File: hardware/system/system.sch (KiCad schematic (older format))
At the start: 20 parts, among them J1 CART_SOCKET_28P, J2 EXT_PINS, SW1 POWER, SW2 RESET, SW3 A, SW4 B, SW5 UP, SW6 DN, SW7 LF, SW8 RT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

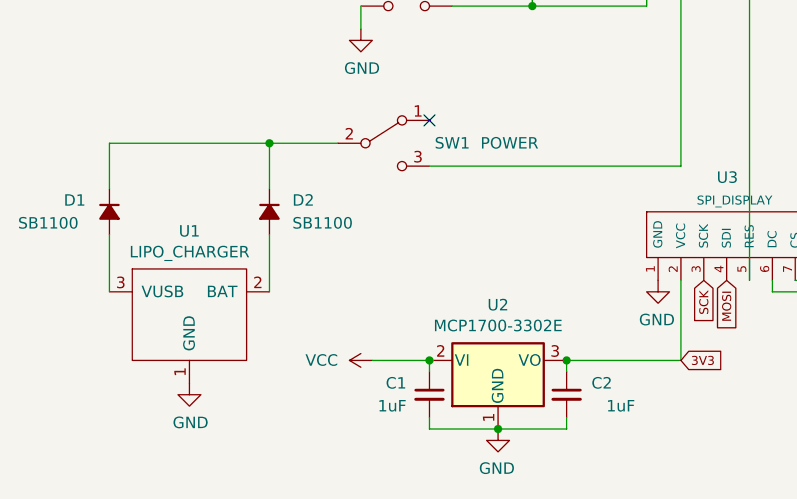
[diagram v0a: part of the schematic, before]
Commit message: Rewire screen regulator Vin to RAW
- Also add schematic PDFs
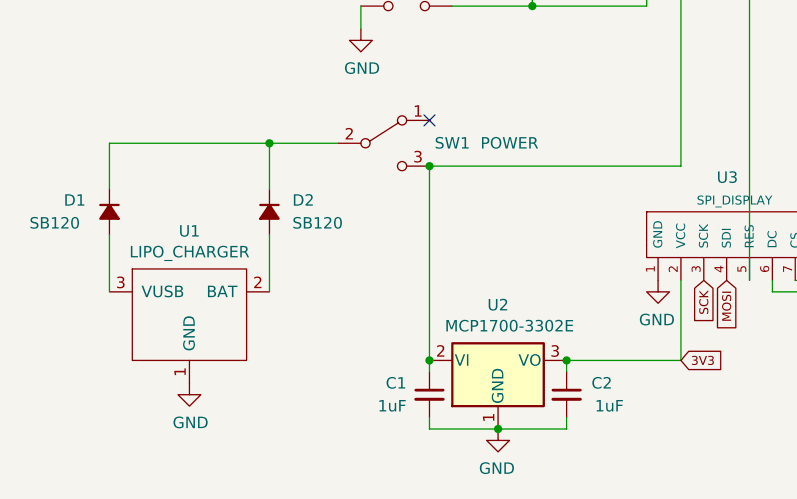
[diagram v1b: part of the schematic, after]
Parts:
- D1, D2: value SB1100 -> SB120
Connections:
- net VCC: no longer C1.1, U2.2 (VI)
- net at J1.26 (Pin_26), SW1.3 (C): now also C1.1, U2.2 (VI)
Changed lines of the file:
@@
 encoding utf-8
 Sheet 1 1
-Title ""
-Date ""
-Rev ""
+Title "Arduboy CE"
+Date "2021-02-12"
+Rev "1.0-dev2"
 Comp ""
 Comment1 ""
@@
 P 4050 5200
 F 0 "U2" H 4050 4958 50  0000 C CNN
-F 1 "MCP1700-3302E" H 4050 5049 50  0000 C CNN
+F 1 "MCP1700-3302E" H 4100 5050 50  0000 C CNN
 F 2 "system:TO-92" H 4050 5000 50  0001 C CIN
 F 3 "http://ww1.microchip.com/downloads/en/DeviceDoc/20001826D.pdf" H 4050 5200 50  0001 C CNN
@@
 P 3050 4550
 F 0 "D2" V 3000 4650 50  0000 L CNN
-F 1 "SB1100" V 3100 4650 50  0000 L CNN
+F 1 "SB120" V 3100 4650 50  0000 L CNN
 F 2 "Diode_THT:D_DO-35_SOD27_P7.62mm_Horizontal" V 3050 4550 50  0001 C CNN
 F 3 "~" V 3050 4550 50  0001 C CNN
@@
 P 2350 4550
 F 0 "D1" V 2300 4750 50  0000 R CNN
-F 1 "SB1100" V 2400 4950 50  0000 R CNN
+F 1 "SB120" V 2400 4900 50  0000 R CNN
 F 2 "Diode_THT:D_DO-35_SOD27_P7.62mm_Horizontal" V 2350 4550 50  0001 C CNN
 F 3 "~" V 2350 4550 50  0001 C CNN
@@
 	1    5050 4650
 	1    0    0    -1
-$EndComp
-$Comp
-L power:VCC #PWR0107
-U 1 1 601937EE
-P 3500 5200
-F 0 "#PWR0107" H 3500 5050 50  0001 C CNN
-F 1 "VCC" V 3500 5350 50  0000 L CNN
-F 2 "" H 3500 5200 50  0001 C CNN
-F 3 "" H 3500 5200 50  0001 C CNN
-	1    3500 5200
-	0    -1   1    0
 $EndComp
 $Comp
@@
 P 4350 5350
 F 0 "C2" H 4550 5400 50  0000 R CNN
-F 1 "1uF" H 4650 5300 50  0000 R CNN
+F 1 "1uF" H 4600 5300 50  0000 R CNN
 F 2 "Capacitor_THT:C_Rect_L4.0mm_W2.5mm_P2.50mm" H 4350 5350 50  0001 C CNN
 F 3 "~" H 4350 5350 50  0001 C CNN
@@
 Wire Wire Line
 	3750 5250 3750 5200
-Wire Wire Line
-	3500 5200 3750 5200
 Connection ~ 3750 5200
 Wire Wire Line
@@
 Text GLabel 8650 3650 3    39   Input ~ 0
 D0
+Connection ~ 3750 4350
+Wire Wire Line
+	3750 4350 3750 5200
 $EndSCHEMATC

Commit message: Connect power to VCC instead of RAW
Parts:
- J2: symbol Connector:Conn_01x11_Female -> Connector:Conn_01x12_Female
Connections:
- net 3V3: now also J2.4 (Pin_4); no longer J2.3 (Pin_3)
- net D0: now also J2.10 (Pin_10); no longer J2.9 (Pin_9)
- net D10_A10: now also J2.12 (Pin_12); no longer J2.11 (Pin_11)
- net D9_A9: now also J2.11 (Pin_11); no longer J2.10 (Pin_10)
- net MISO: now also J2.7 (Pin_7); no longer J2.6 (Pin_6)
- net MOSI: now also J2.8 (Pin_8); no longer J2.7 (Pin_7)
- net SCK: now also J2.9 (Pin_9); no longer J2.8 (Pin_8)
- net SCL: now also J2.6 (Pin_6); no longer J2.5 (Pin_5)
- net SDA: now also J2.5 (Pin_5); no longer J2.4 (Pin_4)
- net VCC: now also C1.1, J2.3 (Pin_3), SW1.3 (C), U2.2 (VI); no longer J2.2 (Pin_2)
- new net RAW: J1.26 (Pin_26), J2.2 (Pin_2)
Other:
- note removed: "RAW"
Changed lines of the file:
@@
 Title "Arduboy CE"
 Date "2021-02-12"
-Rev "1.0-dev2"
+Rev "1.0-dev3"
 Comp ""
 Comment1 ""
@@
 NoConn ~ 6750 4100
 NoConn ~ 6650 4100
-Text Notes 5650 3600 1    39   ~ 0
-RAW
 Text Notes 5850 3600 1    39   ~ 0
 RST
@@
 	1    0    0    -1
 $EndComp
-Wire Wire Line
-	4850 3450 5650 3450
-Wire Wire Line
-	5650 3450 5650 3600
 $Comp
 L power:GND #PWR0104
@@
 D10_A10
 $Comp
-L Connector:Conn_01x11_Female J2
+L Connector:Conn_01x12_Female J2
 U 1 1 6029D390
-P 8350 3450
-F 0 "J2" V 8515 3380 50  0000 C CNN
-F 1 "EXT_PINS" V 8424 3380 50  0000 C CNN
-F 2 "system:EXT_PINS" H 8350 3450 50  0001 C CNN
-F 3 "~" H 8350 3450 50  0001 C CNN
-	1    8350 3450
+P 8250 3450
+F 0 "J2" V 8415 3380 50  0000 C CNN
+F 1 "EXT_PINS" V 8324 3380 50  0000 C CNN
+F 2 "system:EXT_PINS" H 8250 3450 50  0001 C CNN
+F 3 "~" H 8250 3450 50  0001 C CNN
+	1    8250 3450
 	0    -1   -1   0
 $EndComp
@@
 L power:GND #PWR0110
 U 1 1 602A3E9B
-P 7850 3650
-F 0 "#PWR0110" H 7850 3400 50  0001 C CNN
-F 1 "GND" H 7800 3500 50  0000 C CNN
-F 2 "" H 7850 3650 50  0001 C CNN
-F 3 "" H 7850 3650 50  0001 C CNN
-	1    7850 3650
+P 7750 3650
+F 0 "#PWR0110" H 7750 3400 50  0001 C CNN
+F 1 "GND" H 7700 3500 50  0000 C CNN
+F 2 "" H 7750 3650 50  0001 C CNN
+F 3 "" H 7750 3650 50  0001 C CNN
+	1    7750 3650
 	1    0    0    -1
 $EndComp
@@
 Wire Wire Line
 	4200 3650 4700 3650
-Wire Wire Line
-	4850 4350 3750 4350
-Wire Wire Line
-	4850 3450 4850 4350
 Connection ~ 5150 3350
 Wire Wire Line
@@
 Text GLabel 8650 3650 3    39   Input ~ 0
 D0
+Wire Wire Line
+	3750 4350 3750 5200
+Text GLabel 7850 3650 3    39   Input ~ 0
+RAW
+Text GLabel 5650 3600 1    39   Input ~ 0
+RAW
+$Comp
+L power:VCC #PWR?
+U 1 1 6028122A
+P 4250 4350
+F 0 "#PWR?" H 4250 4200 50  0001 C CNN
+F 1 "VCC" V 4250 4500 50  0000 L CNN
+F 2 "" H 4250 4350 50  0001 C CNN
+F 3 "" H 4250 4350 50  0001 C CNN
+	1    4250 4350
+	0    1    1    0
+$EndComp
+Wire Wire Line
+	4250 4350 3750 4350
 Connection ~ 3750 4350
-Wire Wire Line
-	3750 4350 3750 5200
 $EndSCHEMATC

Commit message: Connect display RES to D0/RX
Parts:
- J2: symbol Connector:Conn_01x12_Female -> Connector:Conn_01x11_Female
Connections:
- net D10_A10: now also J2.11 (Pin_11); no longer J2.12 (Pin_12)
- net D9_A9: now also J2.10 (Pin_10); no longer J2.11 (Pin_11)
- net at J1.24 (Pin_24), R1.2, SW2.2: no longer U3.5 (RES)
- net D0: no longer names the net of J1.2 (Pin_2)
- net D0: now also U3.5 (RES); no longer J2.10 (Pin_10)
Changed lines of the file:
@@
 D10_A10
 $Comp
-L Connector:Conn_01x12_Female J2
+L Connector:Conn_01x11_Female J2
 U 1 1 6029D390
 P 8250 3450
@@
 Text GLabel 8550 3650 3    39   Input ~ 0
 SCK
-Text GLabel 8850 3650 3    39   Input ~ 0
+Text GLabel 8750 3650 3    39   Input ~ 0
 D10_A10
-Text GLabel 8750 3650 3    39   Input ~ 0
+Text GLabel 8650 3650 3    39   Input ~ 0
 D9_A9
 Text GLabel 6550 4250 3    39   Input ~ 0
@@
 Wire Wire Line
 	6550 4100 6550 4250
-Wire Wire Line
-	4700 3350 5150 3350
-Wire Wire Line
-	5150 4850 5150 3350
 NoConn ~ 3750 4150
 Wire Wire Line
 	4200 3650 4700 3650
-Connection ~ 5150 3350
-Wire Wire Line
-	5150 3350 5850 3350
-Text GLabel 5550 4250 3    39   Input ~ 0
-D0
-Wire Wire Line
-	5550 4100 5550 4250
-Text GLabel 8650 3650 3    39   Input ~ 0
-D0
 Wire Wire Line
 	3750 4350 3750 5200
@@
 	4250 4350 3750 4350
 Connection ~ 3750 4350
+Wire Wire Line
+	4700 3350 5850 3350
+Wire Wire Line
+	5150 4850 5150 4950
+Wire Wire Line
+	5150 4950 5550 4950
+Wire Wire Line
+	5550 4100 5550 4950
 $EndSCHEMATC

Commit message: Update system and cart
- Shorten cart by 1mm to account for other connector brand
- Use 1-pin header for charger board support
- Fix diode footprint
- Bump cart/system versions (no gerbers yet)
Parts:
- D1, D2: footprint Diode_THT:D_DO-35_SOD27_P7.62mm_Horizontal -> Diode_THT:D_DO-41_SOD81_P7.62mm_Horizontal
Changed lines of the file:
@@
 Sheet 1 1
 Title "Arduboy CE"
-Date "2021-03-04"
-Rev "1.0-dev4"
+Date "2021-04-12"
+Rev "1.0-dev5"
 Comp ""
 Comment1 ""
@@
 F 0 "D2" V 3000 4650 50  0000 L CNN
 F 1 "SB120" V 3100 4650 50  0000 L CNN
-F 2 "Diode_THT:D_DO-35_SOD27_P7.62mm_Horizontal" V 3050 4550 50  0001 C CNN
+F 2 "Diode_THT:D_DO-41_SOD81_P7.62mm_Horizontal" V 3050 4550 50  0001 C CNN
 F 3 "~" V 3050 4550 50  0001 C CNN
 	1    3050 4550
@@
 F 0 "D1" V 2300 4750 50  0000 R CNN
 F 1 "SB120" V 2400 4900 50  0000 R CNN
-F 2 "Diode_THT:D_DO-35_SOD27_P7.62mm_Horizontal" V 2350 4550 50  0001 C CNN
+F 2 "Diode_THT:D_DO-41_SOD81_P7.62mm_Horizontal" V 2350 4550 50  0001 C CNN
 F 3 "~" V 2350 4550 50  0001 C CNN
 	1    2350 4550

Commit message: Remove 3.3V regulator
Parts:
- removed C1, C2: 1uF, Capacitor_THT:C_Rect_L4.0mm_W2.5mm_P2.50mm, symbol Device:C_Small
- removed U2: MCP1700-3302E, system:TO-92, symbol Regulator_Linear:MCP1700-3302E_TO92
- J2: symbol Connector:Conn_01x11_Female -> Connector:Conn_01x10_Female
- renumbered U3 to U2
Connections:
- net D10_A10: now also J2.10 (Pin_10); no longer J2.11 (Pin_11)
- net D9_A9: now also J2.9 (Pin_9); no longer J2.10 (Pin_10)
- net MISO: now also J2.6 (Pin_6); no longer J2.7 (Pin_7)
- net MOSI: now also J2.7 (Pin_7); no longer J2.8 (Pin_8)
- net SCK: now also J2.8 (Pin_8); no longer J2.9 (Pin_9)
- net SCL: now also J2.5 (Pin_5); no longer J2.6 (Pin_6)
- net SDA: now also J2.4 (Pin_4); no longer J2.5 (Pin_5)
- net VCC: now also U2.2 (VCC)
- removed net 3V3: J2.4 (Pin_4), U2.2 (VCC)
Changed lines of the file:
@@
 Sheet 1 1
 Title "Arduboy CE"
-Date "2021-04-12"
+Date "2021-06-07"
 Rev "1.0-dev5"
 Comp ""
@@
 $EndComp
 $Comp
-L Regulator_Linear:MCP1700-3302E_TO92 U2
-U 1 1 60150B9F
-P 4050 5200
-F 0 "U2" H 4050 4958 50  0000 C CNN
-F 1 "MCP1700-3302E" H 4100 5050 50  0000 C CNN
-F 2 "system:TO-92" H 4050 5000 50  0001 C CIN
-F 3 "http://ww1.microchip.com/downloads/en/DeviceDoc/20001826D.pdf" H 4050 5200 50  0001 C CNN
-	1    4050 5200
-	1    0    0    1
-$EndComp
-$Comp
 L system:LIPO_CHARGER U1
 U 1 1 601553BA
@@
 Connection ~ 7500 4950
 $Comp
-L system:SPI_DISPLAY U3
+L system:SPI_DISPLAY U2
 U 1 1 60191D78
 P 5050 4650
-F 0 "U3" H 5100 4900 50  0000 R CNN
+F 0 "U2" H 5100 4900 50  0000 R CNN
 F 1 "SPI_DISPLAY" H 5250 4800 39  0000 R CNN
 F 2 "system:DIYMORE_2.42_IN_OLED" H 5100 4550 30  0001 C CNN
@@
 	1    0    0    -1
 $EndComp
-$Comp
-L power:GND #PWR0108
-U 1 1 6019D0B9
-P 4050 5500
-F 0 "#PWR0108" H 4050 5250 50  0001 C CNN
-F 1 "GND" H 4055 5327 50  0000 C CNN
-F 2 "" H 4050 5500 50  0001 C CNN
-F 3 "" H 4050 5500 50  0001 C CNN
-	1    4050 5500
-	-1   0    0    -1
-$EndComp
-$Comp
-L Device:C_Small C1
-U 1 1 601A4D86
-P 3750 5350
-F 0 "C1" H 3850 5400 50  0000 L CNN
-F 1 "1uF" H 3850 5300 50  0000 L CNN
-F 2 "Capacitor_THT:C_Rect_L4.0mm_W2.5mm_P2.50mm" H 3750 5350 50  0001 C CNN
-F 3 "~" H 3750 5350 50  0001 C CNN
-	1    3750 5350
-	-1   0    0    -1
-$EndComp
-$Comp
-L Device:C_Small C2
-U 1 1 601AE8F3
-P 4350 5350
-F 0 "C2" H 4550 5400 50  0000 R CNN
-F 1 "1uF" H 4600 5300 50  0000 R CNN
-F 2 "Capacitor_THT:C_Rect_L4.0mm_W2.5mm_P2.50mm" H 4350 5350 50  0001 C CNN
-F 3 "~" H 4350 5350 50  0001 C CNN
-	1    4350 5350
-	1    0    0    -1
-$EndComp
-Wire Wire Line
-	3750 5500 4050 5500
-Connection ~ 4050 5500
-Wire Wire Line
-	4050 5500 4350 5500
 $Comp
 L power:GND #PWR0109
@@
 $EndComp
 Wire Wire Line
-	4350 5200 4850 5200
-Wire Wire Line
-	3750 5450 3750 5500
-Wire Wire Line
-	4350 5500 4350 5450
-Wire Wire Line
-	4350 5250 4350 5200
-Connection ~ 4350 5200
-Wire Wire Line
-	3750 5250 3750 5200
-Connection ~ 3750 5200
-Wire Wire Line
 	4850 5200 4850 4850
 Wire Wire Line
@@
 D10_A10
 $Comp
-L Connector:Conn_01x11_Female J2
+L Connector:Conn_01x10_Female J2
 U 1 1 6029D390
-P 8250 3450
-F 0 "J2" V 8415 3380 50  0000 C CNN
-F 1 "EXT_PINS" V 8324 3380 50  0000 C CNN
-F 2 "system:EXT_PINS" H 8250 3450 50  0001 C CNN
-F 3 "~" H 8250 3450 50  0001 C CNN
-	1    8250 3450
+P 8150 3450
+F 0 "J2" V 8315 3380 50  0000 C CNN
+F 1 "EXT_PINS" V 8224 3380 50  0000 C CNN
+F 2 "system:EXT_PINS" H 8150 3450 50  0001 C CNN
+F 3 "~" H 8150 3450 50  0001 C CNN
+	1    8150 3450
 	0    -1   -1   0
 $EndComp
@@
 	1    0    0    1
 $EndComp
-Text GLabel 4850 5200 2    39   Input ~ 0
-3V3
 Text GLabel 8050 3650 3    39   Input ~ 0
-3V3
+SDA
 Text GLabel 8150 3650 3    39   Input ~ 0
-SDA
+SCL
 Text GLabel 8250 3650 3    39   Input ~ 0
-SCL
+MISO
 Text GLabel 8350 3650 3    39   Input ~ 0
-MISO
+MOSI
 Text GLabel 8450 3650 3    39   Input ~ 0
-MOSI
+SCK
+Text GLabel 8650 3650 3    39   Input ~ 0
+D10_A10
 Text GLabel 8550 3650 3    39   Input ~ 0
-SCK
-Text GLabel 8750 3650 3    39   Input ~ 0
-D10_A10
-Text GLabel 8650 3650 3    39   Input ~ 0
 D9_A9
 Text GLabel 6550 4250 3    39   Input ~ 0
@@
 Wire Wire Line
 	4200 3650 4700 3650
-Wire Wire Line
-	3750 4350 3750 5200
 Text GLabel 7850 3650 3    39   Input ~ 0
 RAW
@@
 RAW
 $Comp
-L power:VCC #PWR?
+L power:VCC #PWR0107
 U 1 1 6028122A
 P 4250 4350
-F 0 "#PWR?" H 4250 4200 50  0001 C CNN
+F 0 "#PWR0107" H 4250 4200 50  0001 C CNN
 F 1 "VCC" V 4250 4500 50  0000 L CNN
 F 2 "" H 4250 4350 50  0001 C CNN
@@
 $EndComp
 Wire Wire Line
-	4250 4350 3750 4350
-Connection ~ 3750 4350
+	4250 4350 4100 4350
 Wire Wire Line
 	4700 3350 5850 3350
@@
 Wire Wire Line
 	5550 4100 5550 4950
+Wire Wire Line
+	4850 5200 4100 5200
+Wire Wire Line
+	4100 5200 4100 4350
+Connection ~ 4100 4350
+Wire Wire Line
+	4100 4350 3750 4350
 $EndSCHEMATC
